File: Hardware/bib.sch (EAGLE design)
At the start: 65 parts, among them IC1 7805TV, IC2 7812TV, IC3 LM1117V33TV, IC4 74HC157D

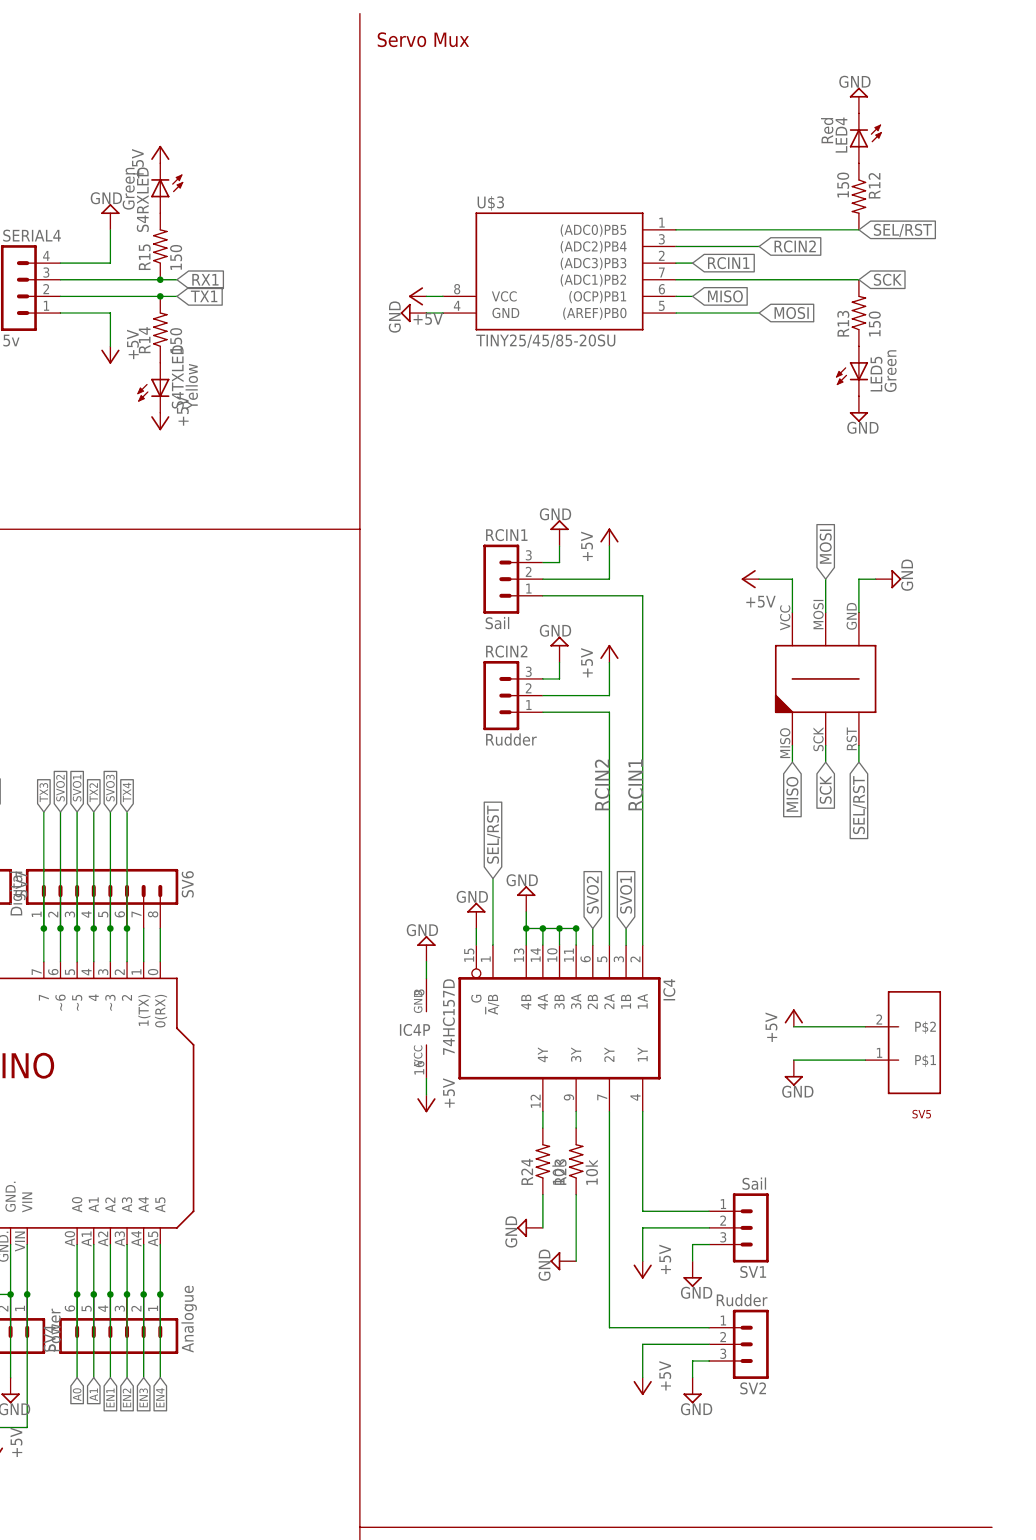
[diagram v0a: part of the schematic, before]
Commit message: fixed errors bringing this up to V1.1
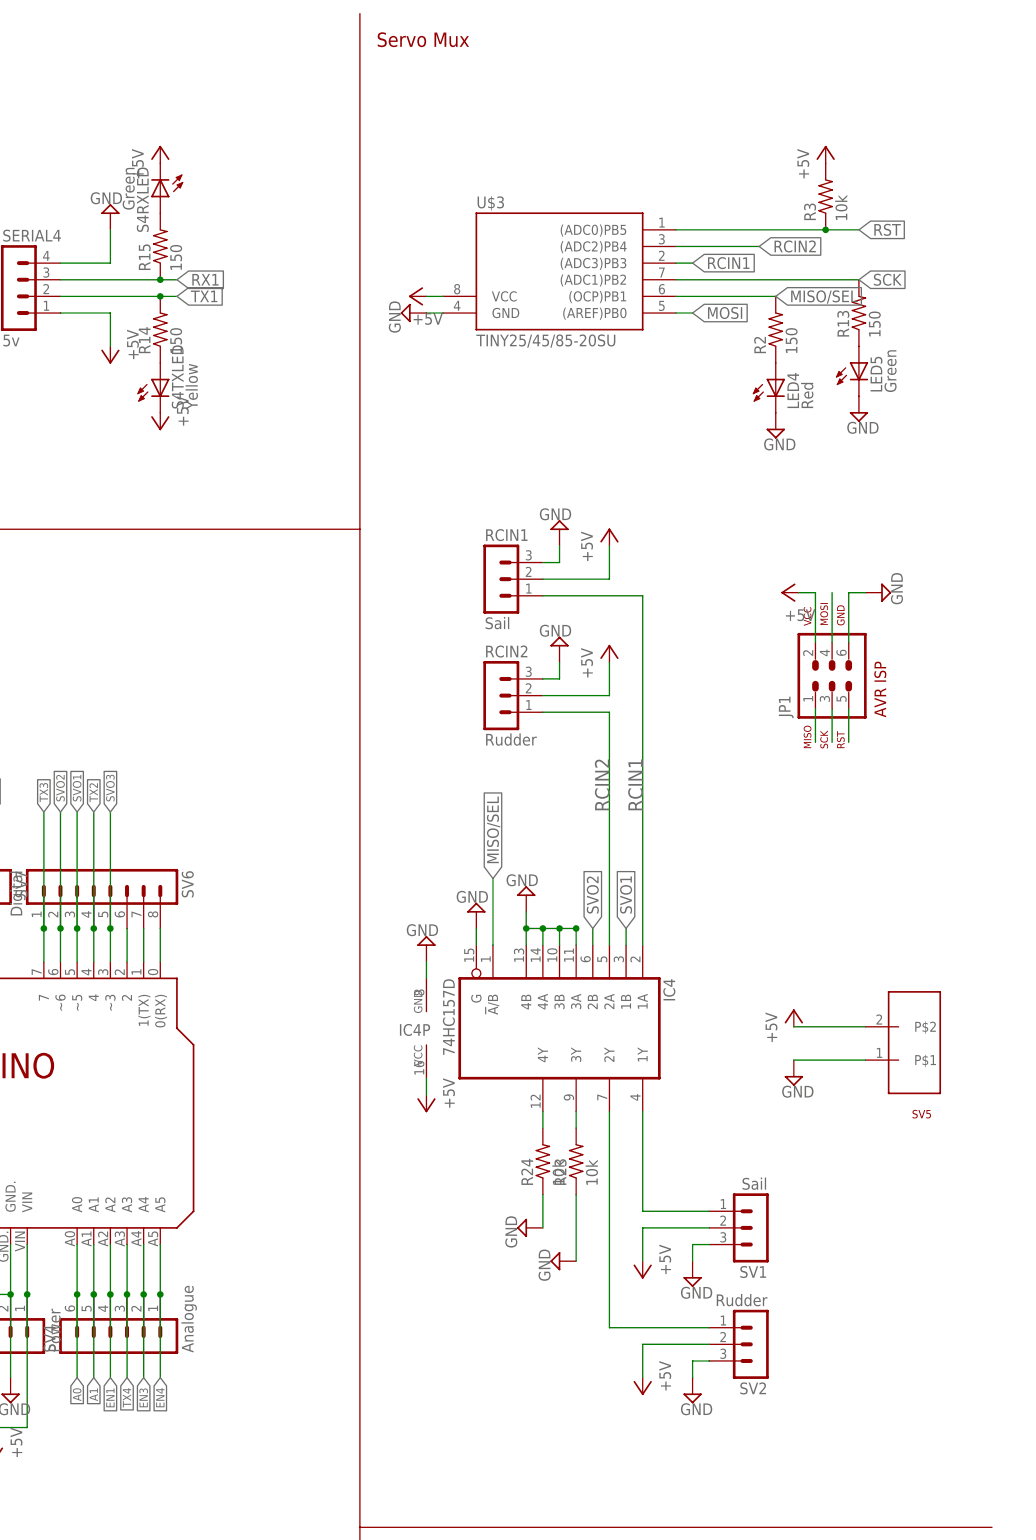
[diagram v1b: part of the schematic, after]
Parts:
- removed R12: 150, resistor:R-US_R0805
- removed U$4: AVR-ISP-6-EDGE, my_lib:AVR-ISP-6-EDGE
- added JP1: AVR-ISP-6VERT, avr-7:AVR-ISP-6VERT
- added R2: 150, resistor:R-US_R0805
- added R3: 10k, resistor:R-US_R0805
- LED4: MPN KPT-3216SRC-J4 -> KPT-3216SGC; OC_FARNELL 2314403 -> 2099247RL
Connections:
- removed net EN2: PCB2.A3, SV4.3
- removed net MISO: U$3.(OCP)PB1, U$4.P$1
- removed net N$33: LED4.A, R12.1
- removed net SEL/RST: IC4A.!A!/B, R12.2, U$3.(ADC0)PB5, U$4.P$3
- new net MEH: PCB2.2, SV6.6
- new net MISO/SEL: IC4A.!A!/B, JP1.1, R2.2, U$3.(OCP)PB1
- new net N$2: LED4.A, R2.1
- new net RST: JP1.5, R3.1, U$3.(ADC0)PB5
- net +5V: now also JP1.2, R3.2; no longer U$4.P$6
- net GND: now also JP1.6; no longer U$4.P$4
- net MOSI: now also JP1.4; no longer U$4.P$5
- net SCK: now also JP1.3; no longer U$4.P$2
- net TX4: now also PCB2.A3, SV4.3; no longer PCB2.2, SV6.6
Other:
- moved on the sheet: LED4
